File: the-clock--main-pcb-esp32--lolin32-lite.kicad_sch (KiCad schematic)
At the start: 15 parts, among them J1 Conn_01x04, SW1 SW_Push, SW2 SW_Push, SW3 SW_Push, SW4 SW_Push

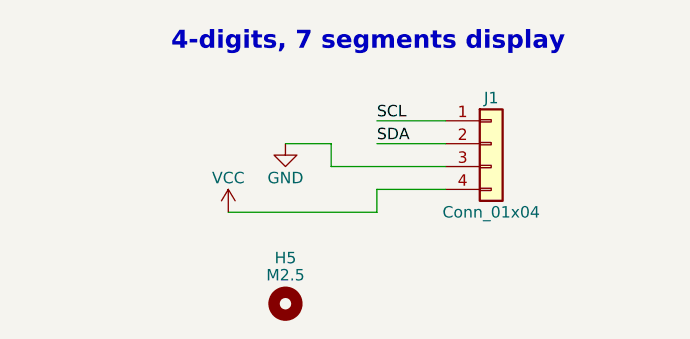
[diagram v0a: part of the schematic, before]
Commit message: remove useless hole (already included by the footprint)
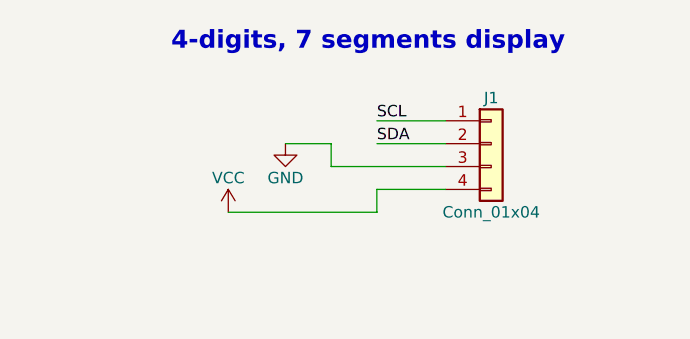
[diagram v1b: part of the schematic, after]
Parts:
- removed H5: M2.5, symbol Mechanical:MountingHole
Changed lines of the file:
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@@
-    )
-  )
-  (symbol (lib_id "Mechanical:MountingHole") (at 50.8 129.54 0) (unit 1)
-    (in_bom yes) (on_board yes) (dnp no)
-    (property "Reference" "H5" (at 50.8 124.46 0)
-      (effects (font (size 1.27 1.27)))
-    )
-    (property "Value" "M2.5" (at 50.8 126.365 0)
-      (effects (font (size 1.27 1.27)))
-    )
-    (property "Footprint" "" (at 50.8 129.54 0)
-      (effects (font (size 1.27 1.27)) hide)
-    )
-    (property "Datasheet" "~" (at 50.8 129.54 0)
-      (effects (font (size 1.27 1.27)) hide)
-    )
-    (instances
-      (project "the-clock--main-pcb-esp32--lolin32-lite"
-        (path "/dfc91cd7-0548-4b37-8d64-94d7833ed062"
-          (reference "H5") (unit 1)
-        )
-      )
     )
   )

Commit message: assigned footprints
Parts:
- A1: footprint (none) -> assemblies_uc_boards:DIP-26_900_WEMOS_LOLIN32_LITE
- H1, H2, H3, H4: footprint (none) -> MountingHole:MountingHole_2.7mm_M2.5
- J1: footprint (none) -> assemblies_displays_modules:TM1637_7_segments_4_digits_clock_i2c
- R1, R2, R3, R4: footprint (none) -> commons-passives_THT:Passive_THT_resistor_W2.54mm_L10.16mm
- SW1, SW2, SW3, SW4: footprint (none) -> Button_Switch_THT:SW_PUSH_6mm_H13mm
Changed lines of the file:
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@@
       (effects (font (size 1.27 1.27)))
     )
-    (property "Footprint" "" (at 152.4 114.3 0)
+    (property "Footprint" "MountingHole:MountingHole_2.7mm_M2.5" (at 152.4 114.3 0)
       (effects (font (size 1.27 1.27)) hide)
     )
@@
       (effects (font (size 1.27 1.27)))
     )
-    (property "Footprint" "" (at 73.66 111.76 0)
+    (property "Footprint" "assemblies_displays_modules:TM1637_7_segments_4_digits_clock_i2c" (at 73.66 111.76 0)
       (effects (font (size 1.27 1.27)) hide)
     )
@@
       (effects (font (size 1.27 1.27)))
     )
-    (property "Footprint" "" (at 152.4 64.77 0)
+    (property "Footprint" "Button_Switch_THT:SW_PUSH_6mm_H13mm" (at 152.4 64.77 0)
       (effects (font (size 1.27 1.27)) hide)
     )
@@
       (effects (font (size 1.27 1.27) bold) (justify left top))
     )
-    (property "Footprint" "" (at 59.69 63.5 0)
+    (property "Footprint" "assemblies_uc_boards:DIP-26_900_WEMOS_LOLIN32_LITE" (at 59.69 63.5 0)
       (effects (font (size 1.27 1.27)) hide)
     )
@@
       (effects (font (size 1.27 1.27)))
     )
-    (property "Footprint" "" (at 139.7 114.3 0)
+    (property "Footprint" "MountingHole:MountingHole_2.7mm_M2.5" (at 139.7 114.3 0)
       (effects (font (size 1.27 1.27)) hide)
     )
@@
       (effects (font (size 1.27 1.27)))
     )
-    (property "Footprint" "" (at 152.4 52.07 0)
+    (property "Footprint" "Button_Switch_THT:SW_PUSH_6mm_H13mm" (at 152.4 52.07 0)
       (effects (font (size 1.27 1.27)) hide)
     )
@@
       (effects (font (size 1.27 1.27)))
     )
-    (property "Footprint" "" (at 165.1 114.3 0)
+    (property "Footprint" "MountingHole:MountingHole_2.7mm_M2.5" (at 165.1 114.3 0)
       (effects (font (size 1.27 1.27)) hide)
     )
@@
       (effects (font (size 1.27 1.27)) (justify right))
     )
-    (property "Footprint" "" (at 171.45 57.15 0)
+    (property "Footprint" "commons-passives_THT:Passive_THT_resistor_W2.54mm_L10.16mm" (at 171.45 57.15 0)
       (effects (font (size 1.27 1.27)) hide)
     )
@@
       (effects (font (size 1.27 1.27)) (justify right))
     )
-    (property "Footprint" "" (at 171.45 69.85 0)
+    (property "Footprint" "commons-passives_THT:Passive_THT_resistor_W2.54mm_L10.16mm" (at 171.45 69.85 0)
       (effects (font (size 1.27 1.27)) hide)
     )
@@
       (effects (font (size 1.27 1.27)))
     )
-    (property "Footprint" "" (at 152.4 77.47 0)
+    (property "Footprint" "Button_Switch_THT:SW_PUSH_6mm_H13mm" (at 152.4 77.47 0)
       (effects (font (size 1.27 1.27)) hide)
     )
@@
       (effects (font (size 1.27 1.27)))
     )
-    (property "Footprint" "" (at 152.4 39.37 0)
+    (property "Footprint" "Button_Switch_THT:SW_PUSH_6mm_H13mm" (at 152.4 39.37 0)
       (effects (font (size 1.27 1.27)) hide)
     )
@@
       (effects (font (size 1.27 1.27)) (justify right))
     )
-    (property "Footprint" "" (at 171.45 44.45 0)
+    (property "Footprint" "commons-passives_THT:Passive_THT_resistor_W2.54mm_L10.16mm" (at 171.45 44.45 0)
       (effects (font (size 1.27 1.27)) hide)
     )
@@
       (effects (font (size 1.27 1.27)) (justify right))
     )
-    (property "Footprint" "" (at 171.45 82.55 0)
+    (property "Footprint" "commons-passives_THT:Passive_THT_resistor_W2.54mm_L10.16mm" (at 171.45 82.55 0)
       (effects (font (size 1.27 1.27)) hide)
     )
@@
       (effects (font (size 1.27 1.27)))
     )
-    (property "Footprint" "" (at 177.8 114.3 0)
-      (effects (font (size 1.27 1.27)) hide)
-    )
+    (property "Footprint" "MountingHole:MountingHole_2.7mm_M2.5" (at 177.8 114.3 0)
+      (effects (font (size 1.27 1.27)) hide)
+    )

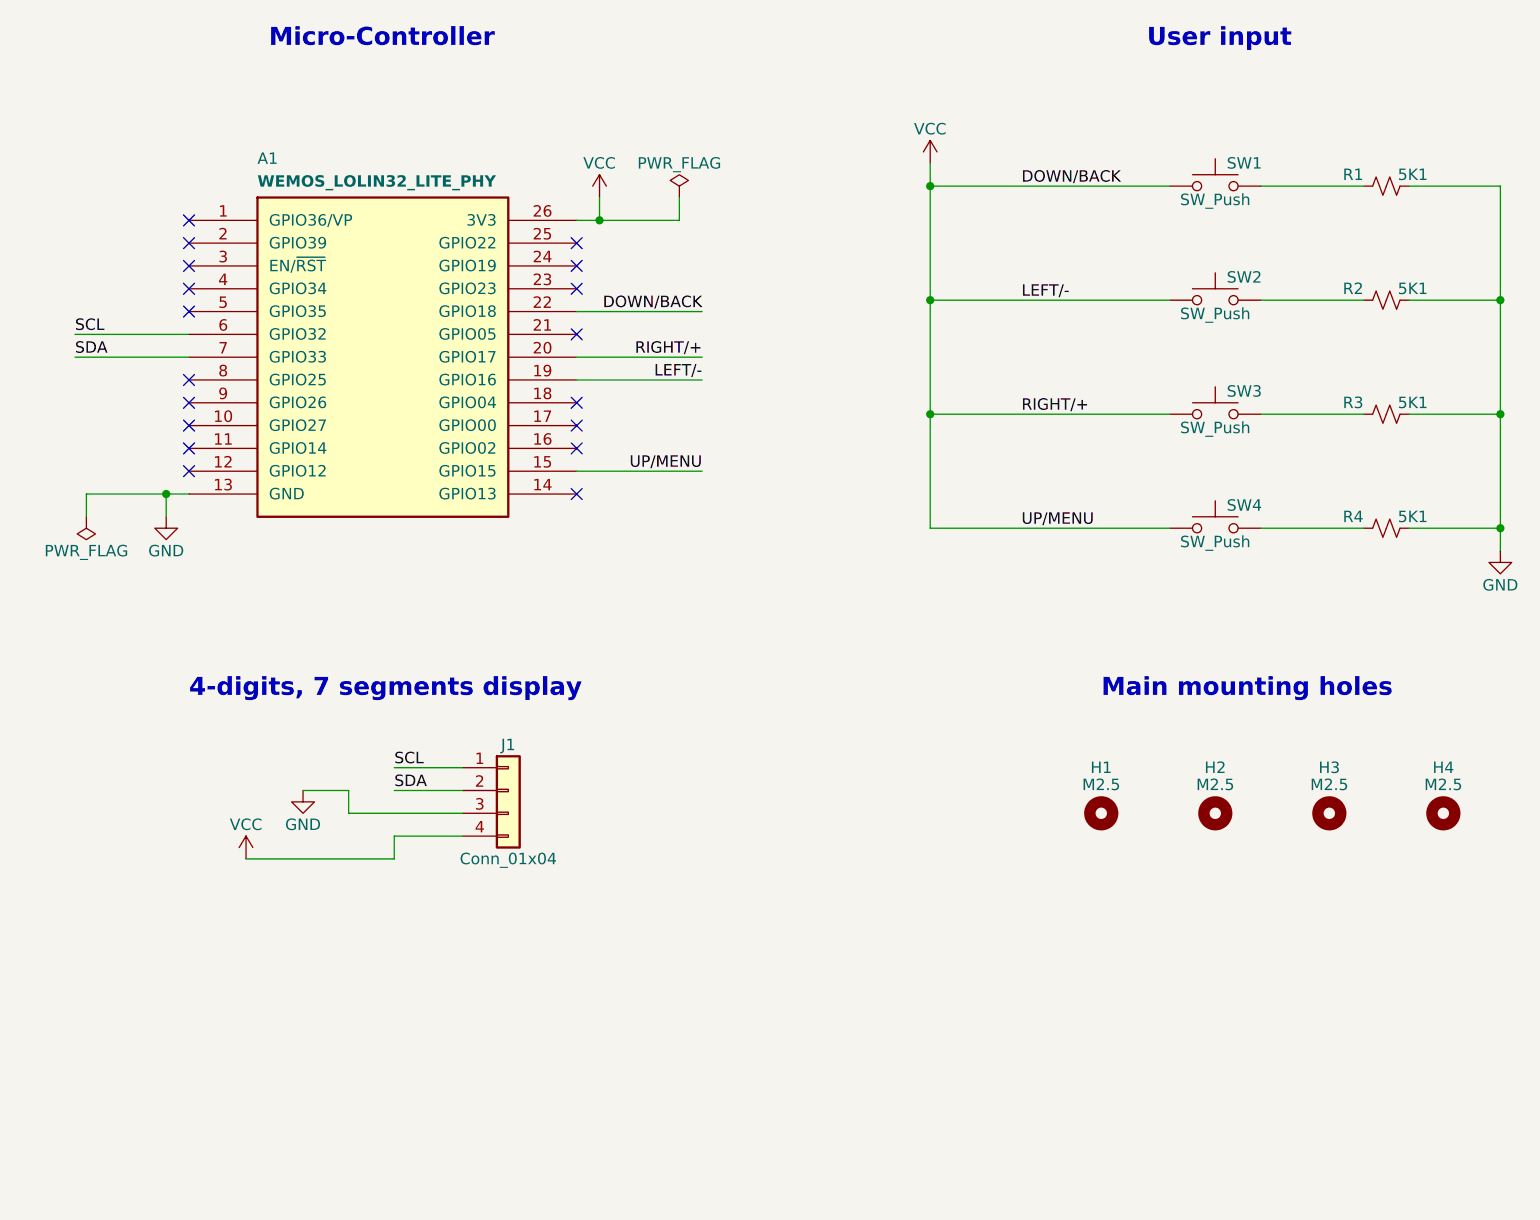
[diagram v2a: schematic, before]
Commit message: fix user input and pull-ups
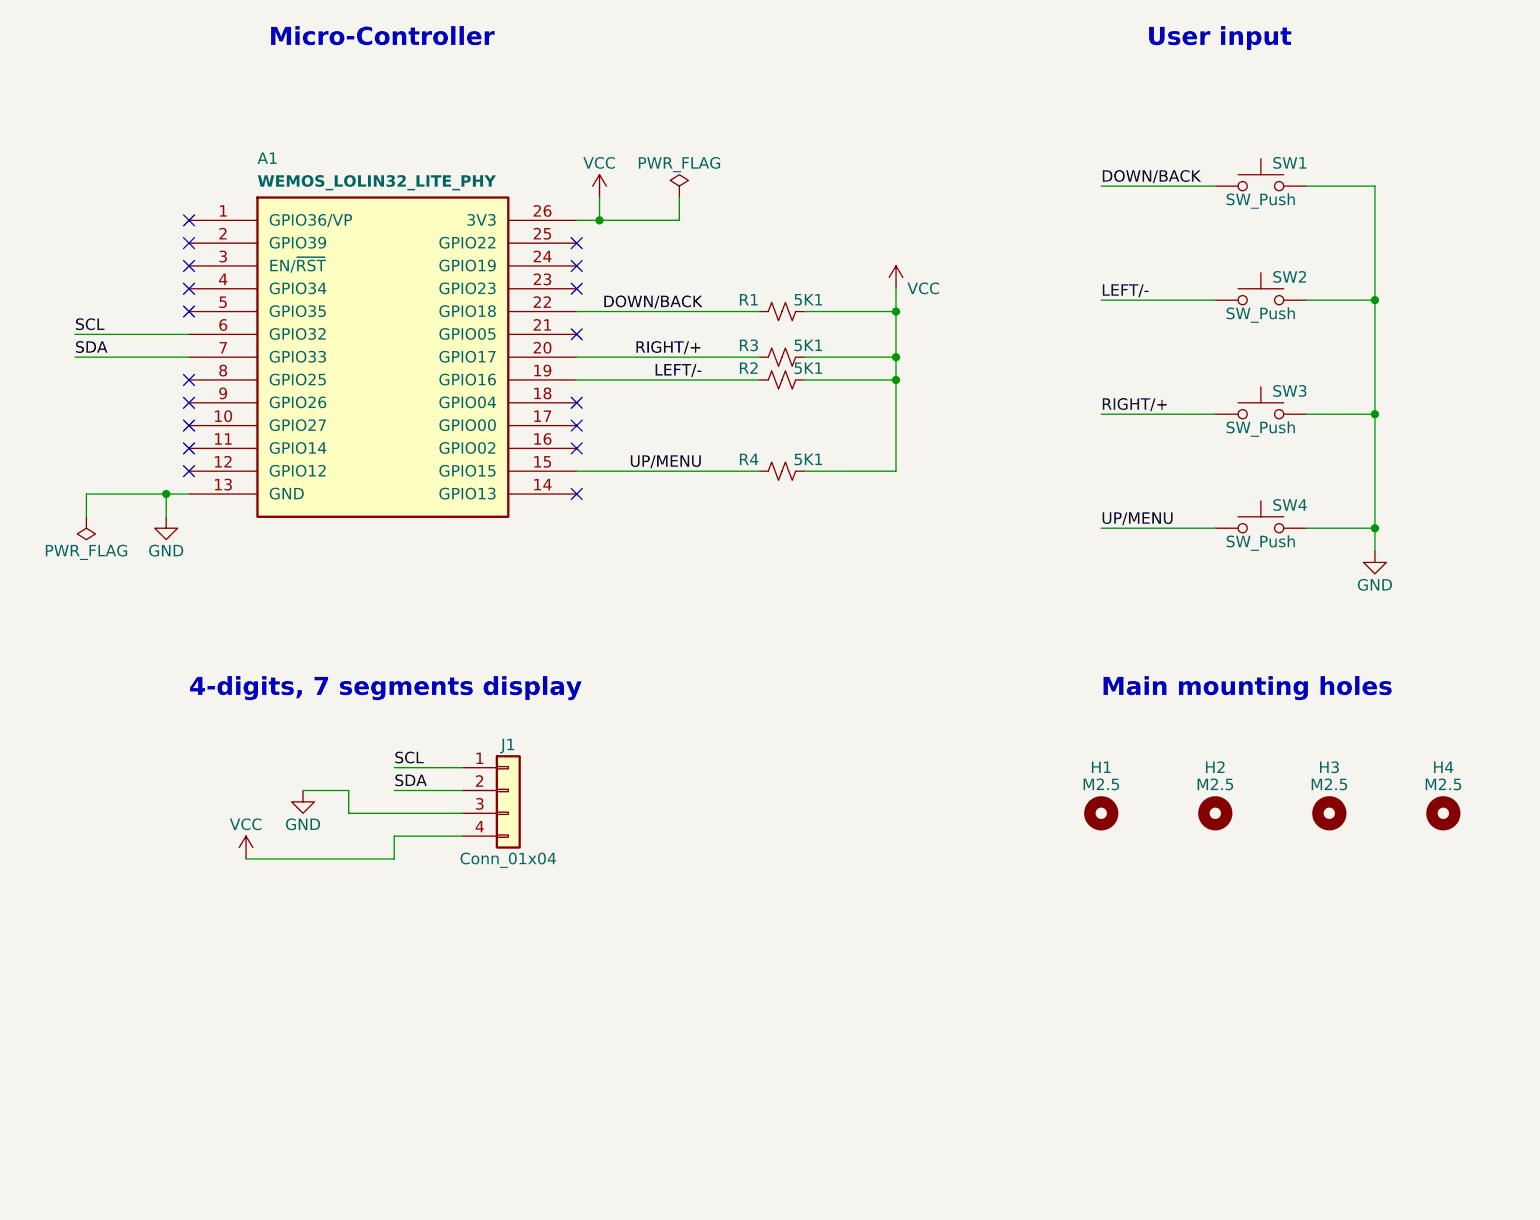
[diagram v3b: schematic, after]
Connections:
- net GND: now also SW1.2, SW2.2, SW3.2, SW4.2; no longer R1.2, R2.2, R3.2, R4.2
- net VCC: now also R1.2, R2.2, R3.2, R4.2; no longer A1.15 (GPIO15), A1.19 (GPIO16), A1.20 (GPIO17), A1.22 (GPIO18), SW1.1, SW2.1, SW3.1, SW4.1
- net RIGHT/+: now reaches R3.1
- net RIGHT/+: now also A1.20 (GPIO17), SW3.1; no longer SW3.2
- net LEFT/-: now reaches R2.1
- net LEFT/-: now also A1.19 (GPIO16), SW2.1; no longer SW2.2
- net UP/MENU: now reaches R4.1
- net UP/MENU: now also A1.15 (GPIO15), SW4.1; no longer SW4.2
- net DOWN/BACK: now reaches R1.1
- net DOWN/BACK: now also A1.22 (GPIO18), SW1.1; no longer SW1.2
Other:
- moved on the sheet: R1, R2, R3, R4, SW1, SW2, SW3, SW4
